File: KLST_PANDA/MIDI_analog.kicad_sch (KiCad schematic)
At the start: 10 parts, among them J3 MIDI_IN, J3 MIDI_OUT, U1 H11L1SR2M, U10 74AHC1G125

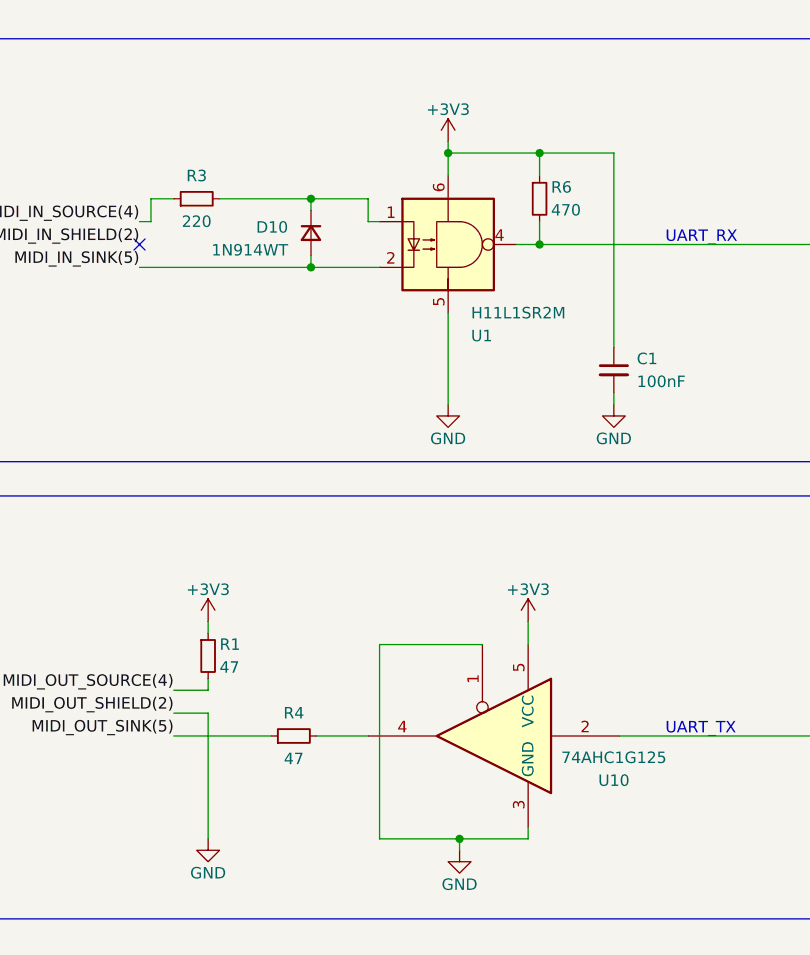
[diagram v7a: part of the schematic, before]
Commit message: removed DRC warnings and error, added power page
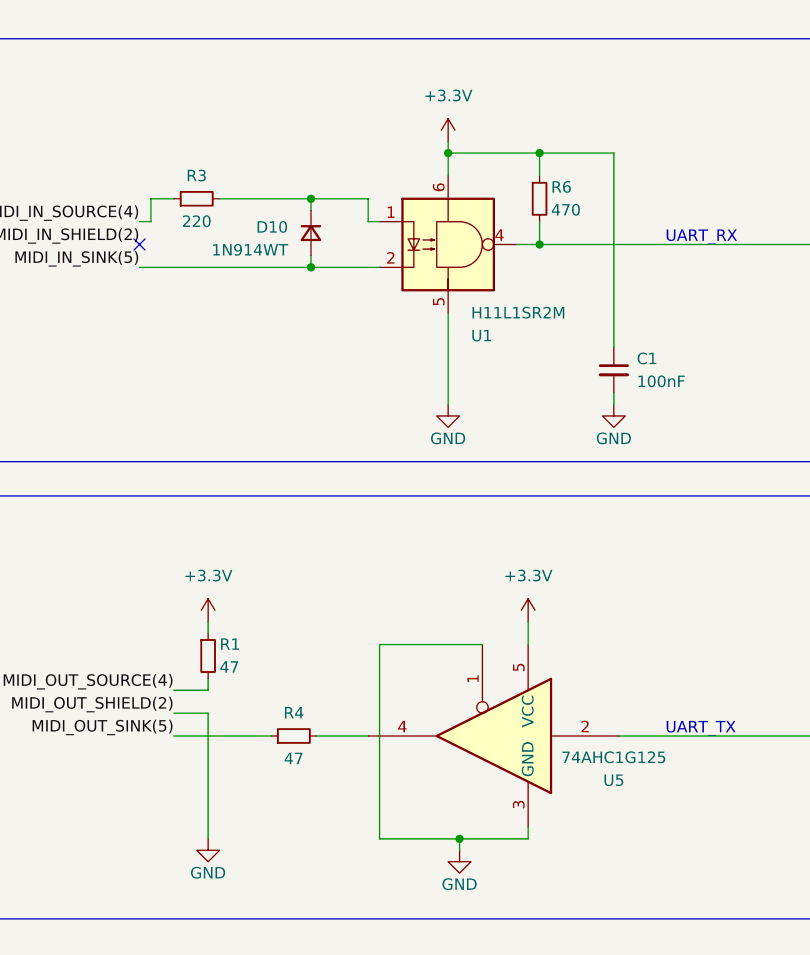
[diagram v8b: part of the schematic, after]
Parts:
- renumbered U10 to U5
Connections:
- net +3V3 renamed +3.3V
